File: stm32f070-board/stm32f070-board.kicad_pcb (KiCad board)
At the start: 2 copper layers, 69.6 x 31.5 mm, 39 parts, among them J1 USB_B_Micro, J2 USB_B_Micro, J3 Conn_01x05_Male, SW1 SW_DPDT_x2, SW2 SW_Push, SW3 SW_Push, U1 CH340G, U2 STM32F070F6P6, U3 MCP9700AT-ETT, U4 Si7055-A20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

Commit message: increased the width of ground and vcc tracks - added net classes
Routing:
- net VCC: track 128.4 -> 129.6 mm
- net Net-(C6-Pad1): track 16.4 -> 17.4 mm
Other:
- net class GND_TRACK added: clearance 0.254, trace_width 0.381, via_dia 0.762, via_drill 0.381
- net class VCC_TRACK added: clearance 0.254, trace_width 0.381, via_dia 0.762, via_drill 0.381

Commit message: exported gerber files
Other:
- board text added: "STM32F070 Board"
- board text removed: "STM32F070 Dev Kit"
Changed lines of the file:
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@@
   (layers
     (0 F.Cu signal)
-    (31 B.Cu signal)
+    (31 B.Cu signal hide)
     (32 B.Adhes user hide)
     (33 F.Adhes user hide)
@@
     (pcbplotparams
       (layerselection 0x010fc_ffffffff)
-      (usegerberextensions false)
+      (usegerberextensions true)
       (usegerberattributes false)
       (usegerberadvancedattributes false)
@@
       (outputformat 1)
       (mirror false)
-      (drillshape 1)
+      (drillshape 0)
       (scaleselection 1)
-      (outputdirectory ""))
+      (outputdirectory "manufacturing/gerbers/"))
   )
   (net 0 "")
@@
     (effects (font (size 0.762 0.762) (thickness 0.1524)))
   )
-  (gr_text "STM32F070 Dev Kit\n\n" (at 104.14 92.202) (layer F.SilkS)
+  (gr_text "STM32F070 Board\n\n" (at 104.14 92.202) (layer F.SilkS)
     (effects (font (size 1.016 1.016) (thickness 0.1524)))
   )

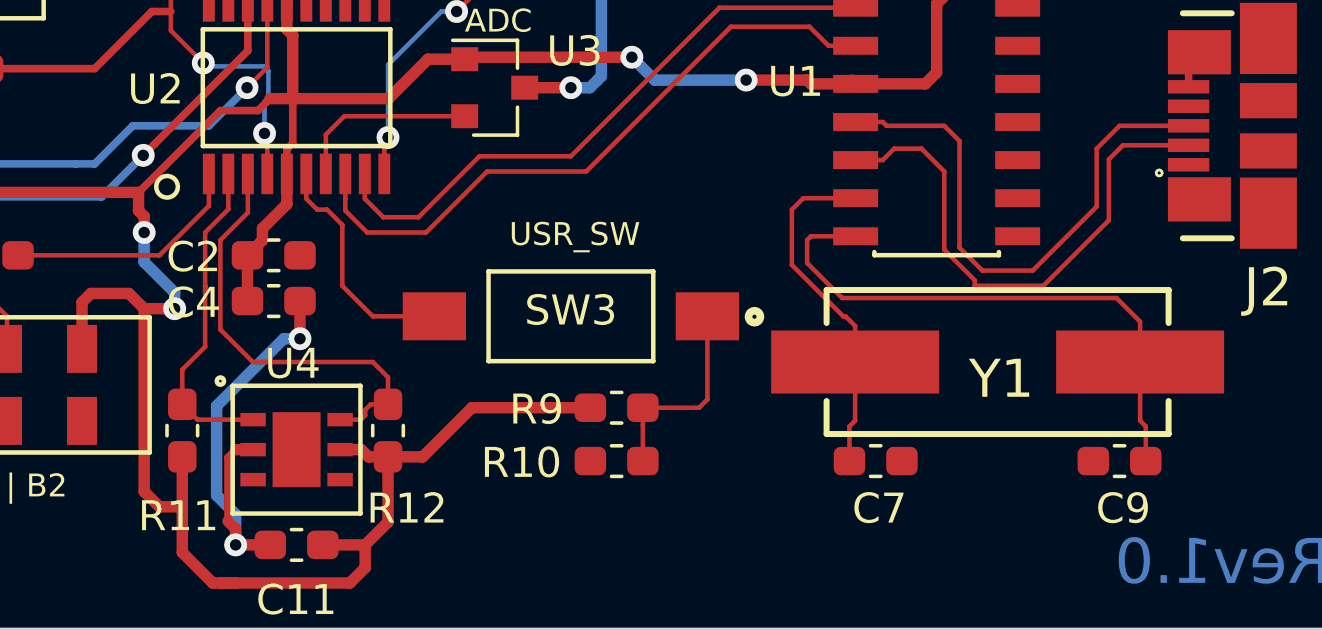
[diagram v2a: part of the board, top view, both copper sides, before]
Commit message: fixed wigly traces on scl line and near the crystal of ch340
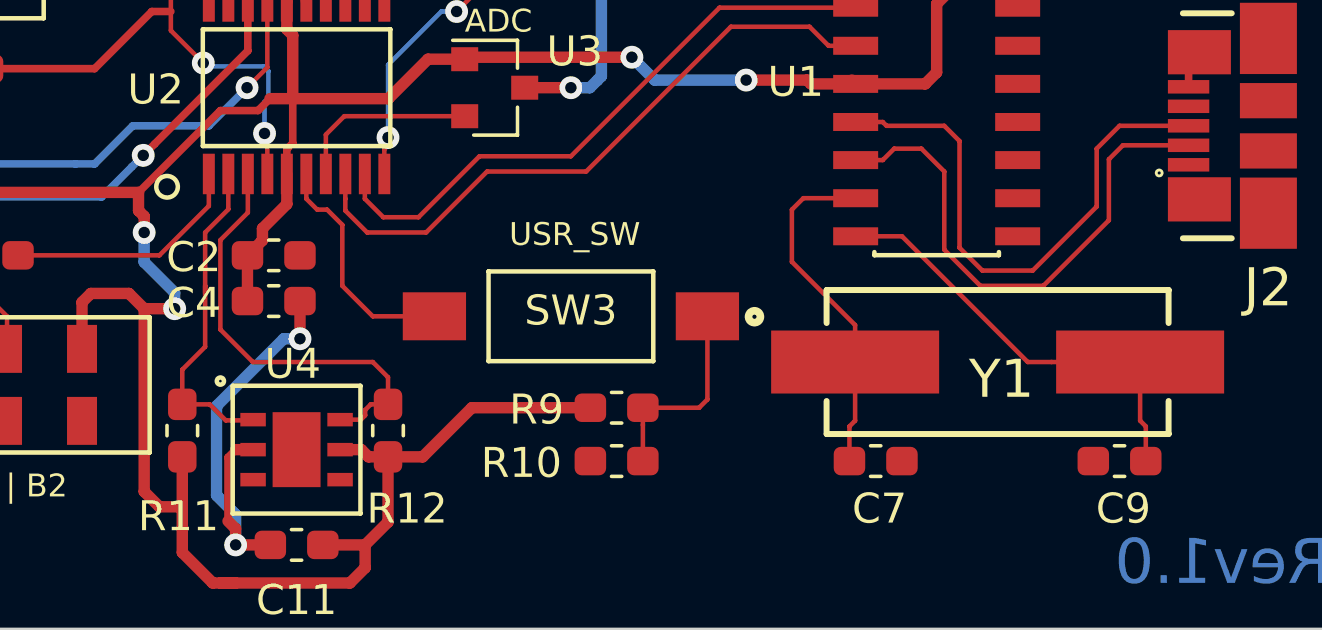
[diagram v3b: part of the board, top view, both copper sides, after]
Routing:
- net Net-(C9-Pad1): track 19.1 -> 14.6 mm
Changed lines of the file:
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@@
     (thickness 1.6)
     (drawings 19)
-    (tracks 399)
+    (tracks 395)
     (zones 0)
     (modules 39)
@@
   (segment (start 111.2012 101.473) (end 111.633 101.9048) (width 0.381) (layer F.Cu) (net 3))
   (segment (start 111.633 101.9048) (end 111.633 102.2096) (width 0.381) (layer F.Cu) (net 3))
-  (segment (start 147.269 108.9701) (end 147.269 110.1725) (width 0.1524) (layer F.Cu) (net 4))
-  (segment (start 147.287 104.7115) (end 145.542 104.7115) (width 0.1524) (layer F.Cu) (net 4))
-  (segment (start 145.161 105.0925) (end 145.161 106.93725) (width 0.1524) (layer F.Cu) (net 4))
-  (segment (start 145.542 104.7115) (end 145.161 105.0925) (width 0.1524) (layer F.Cu) (net 4))
-  (segment (start 145.161 106.93725) (end 146.87225 108.6485) (width 0.1524) (layer F.Cu) (net 4))
-  (segment (start 146.87225 108.6485) (end 146.9474 108.6485) (width 0.1524) (layer F.Cu) (net 4))
-  (segment (start 146.9474 108.6485) (end 147.269 108.9701) (width 0.1524) (layer F.Cu) (net 4))
   (segment (start 147.08 113.4745) (end 147.08 112.3175) (width 0.1524) (layer F.Cu) (net 4))
   (segment (start 147.269 112.1285) (end 147.269 110.1725) (width 0.1524) (layer F.Cu) (net 4))
   (segment (start 147.08 112.3175) (end 147.269 112.1285) (width 0.1524) (layer F.Cu) (net 4))
+  (segment (start 147.269 108.9404) (end 147.269 110.1725) (width 0.1524) (layer F.Cu) (net 4))
+  (segment (start 145.161 106.8324) (end 147.269 108.9404) (width 0.1524) (layer F.Cu) (net 4))
+  (segment (start 145.161 105.0925) (end 145.161 106.8324) (width 0.1524) (layer F.Cu) (net 4))
+  (segment (start 147.287 104.7115) (end 145.542 104.7115) (width 0.1524) (layer F.Cu) (net 4))
+  (segment (start 145.542 104.7115) (end 145.161 105.0925) (width 0.1524) (layer F.Cu) (net 4))
   (via (at 125.541361 100.204861) (size 0.762) (drill 0.381) (layers F.Cu B.Cu) (net 5))
   (segment (start 125.541361 100.204861) (end 124.46 99.1235) (width 0.1524) (layer F.Cu) (net 5))
@@
   (segment (start 127.582622 101.498456) (end 127.711201 101.369877) (width 0.1524) (layer B.Cu) (net 5))
   (segment (start 127.582622 102.5525) (end 127.582622 101.498456) (width 0.1524) (layer B.Cu) (net 5))
-  (segment (start 147.287 105.9815) (end 145.796 105.9815) (width 0.1524) (layer F.Cu) (net 6))
-  (segment (start 145.796 105.9815) (end 145.669 106.1085) (width 0.1524) (layer F.Cu) (net 6))
-  (segment (start 145.669 106.1085) (end 145.669 106.8705) (width 0.1524) (layer F.Cu) (net 6))
-  (segment (start 146.83741 108.03891) (end 155.98141 108.03891) (width 0.1524) (layer F.Cu) (net 6))
-  (segment (start 145.669 106.8705) (end 146.83741 108.03891) (width 0.1524) (layer F.Cu) (net 6))
-  (segment (start 156.769 108.8265) (end 156.769 110.1725) (width 0.1524) (layer F.Cu) (net 6))
-  (segment (start 155.98141 108.03891) (end 156.769 108.8265) (width 0.1524) (layer F.Cu) (net 6))
   (segment (start 156.958 113.4745) (end 156.958 112.3175) (width 0.1524) (layer F.Cu) (net 6))
   (segment (start 156.769 112.1285) (end 156.769 110.1725) (width 0.1524) (layer F.Cu) (net 6))
   (segment (start 156.958 112.3175) (end 156.769 112.1285) (width 0.1524) (layer F.Cu) (net 6))
+  (segment (start 153.8166 110.1725) (end 156.769 110.1725) (width 0.1524) (layer F.Cu) (net 6))
+  (segment (start 153.0223 110.1725) (end 153.8166 110.1725) (width 0.1524) (layer F.Cu) (net 6))
+  (segment (start 147.287 105.9815) (end 148.8313 105.9815) (width 0.1524) (layer F.Cu) (net 6))
+  (segment (start 148.8313 105.9815) (end 153.0223 110.1725) (width 0.1524) (layer F.Cu) (net 6))
   (segment (start 106.92 110.5535) (end 109.765 110.5535) (width 0.254) (layer F.Cu) (net 7))
   (segment (start 132.715 93.9535) (end 132.715 92.2515) (width 0.1524) (layer F.Cu) (net 8))
@@
   (segment (start 125.603 105.8545) (end 125.603 107.6325) (width 0.1524) (layer F.Cu) (net 27))
   (segment (start 125.603 107.6325) (end 125.603 107.8865) (width 0.1524) (layer F.Cu) (net 27))
-  (segment (start 125.351 112.0935) (end 127.201 112.0935) (width 0.1524) (layer F.Cu) (net 27))
-  (segment (start 124.841 111.5835) (end 125.351 112.0935) (width 0.1524) (layer F.Cu) (net 27))
   (segment (start 124.841 110.4265) (end 124.841 111.5835) (width 0.1524) (layer F.Cu) (net 27))
   (segment (start 125.603 107.6325) (end 125.603 109.6645) (width 0.1524) (layer F.Cu) (net 27))
   (segment (start 125.603 109.6645) (end 124.841 110.4265) (width 0.1524) (layer F.Cu) (net 27))
+  (segment (start 127.176916 112.117584) (end 127.201 112.0935) (width 0.1524) (layer F.Cu) (net 27))
+  (segment (start 126.290784 112.117584) (end 127.176916 112.117584) (width 0.1524) (layer F.Cu) (net 27))
+  (segment (start 124.841 111.5835) (end 125.7567 111.5835) (width 0.1524) (layer F.Cu) (net 27))
+  (segment (start 125.7567 111.5835) (end 126.290784 112.117584) (width 0.1524) (layer F.Cu) (net 27))
   (segment (start 130.101 112.0935) (end 130.794 112.0935) (width 0.1524) (layer F.Cu) (net 28))
   (segment (start 130.794 112.0935) (end 130.937 111.9505) (width 0.1524) (layer F.Cu) (net 28))
@@
   (segment (start 156.195 102.9485) (end 158.385 102.9485) (width 0.1524) (layer F.Cu) (net 46))
   (segment (start 155.72741 103.41609) (end 156.195 102.9485) (width 0.1524) (layer F.Cu) (net 46))
+  (segment (start 155.72741 105.44809) (end 155.72741 103.41609) (width 0.1524) (layer F.Cu) (net 46))
   (segment (start 153.543 107.6325) (end 155.72741 105.44809) (width 0.1524) (layer F.Cu) (net 46))
-  (segment (start 151.257 107.6325) (end 153.543 107.6325) (width 0.1524) (layer F.Cu) (net 46))
-  (segment (start 151.257 107.44525) (end 151.257 107.6325) (width 0.1524) (layer F.Cu) (net 46))
+  (segment (start 151.44425 107.6325) (end 153.543 107.6325) (width 0.1524) (layer F.Cu) (net 46))
+  (segment (start 148.1894 103.4415) (end 148.5704 103.0605) (width 0.1524) (layer F.Cu) (net 46))
   (segment (start 147.287 103.4415) (end 148.1894 103.4415) (width 0.1524) (layer F.Cu) (net 46))
-  (segment (start 155.72741 105.44809) (end 155.72741 103.41609) (width 0.1524) (layer F.Cu) (net 46))
   (segment (start 148.5704 103.0605) (end 149.479 103.0605) (width 0.1524) (layer F.Cu) (net 46))
   (segment (start 149.479 103.0605) (end 150.241 103.8225) (width 0.1524) (layer F.Cu) (net 46))
   (segment (start 150.241 103.8225) (end 150.241 106.42925) (width 0.1524) (layer F.Cu) (net 46))
-  (segment (start 148.1894 103.4415) (end 148.5704 103.0605) (width 0.1524) (layer F.Cu) (net 46))
-  (segment (start 150.241 106.42925) (end 151.257 107.44525) (width 0.1524) (layer F.Cu) (net 46))
+  (segment (start 150.241 106.42925) (end 151.44425 107.6325) (width 0.1524) (layer F.Cu) (net 46))
   (zone (net 2) (net_name GND) (layer F.Cu) (hatch edge 0.508)
     (connect_pads (clearance 0.508))
